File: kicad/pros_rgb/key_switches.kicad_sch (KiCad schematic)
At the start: 0 parts

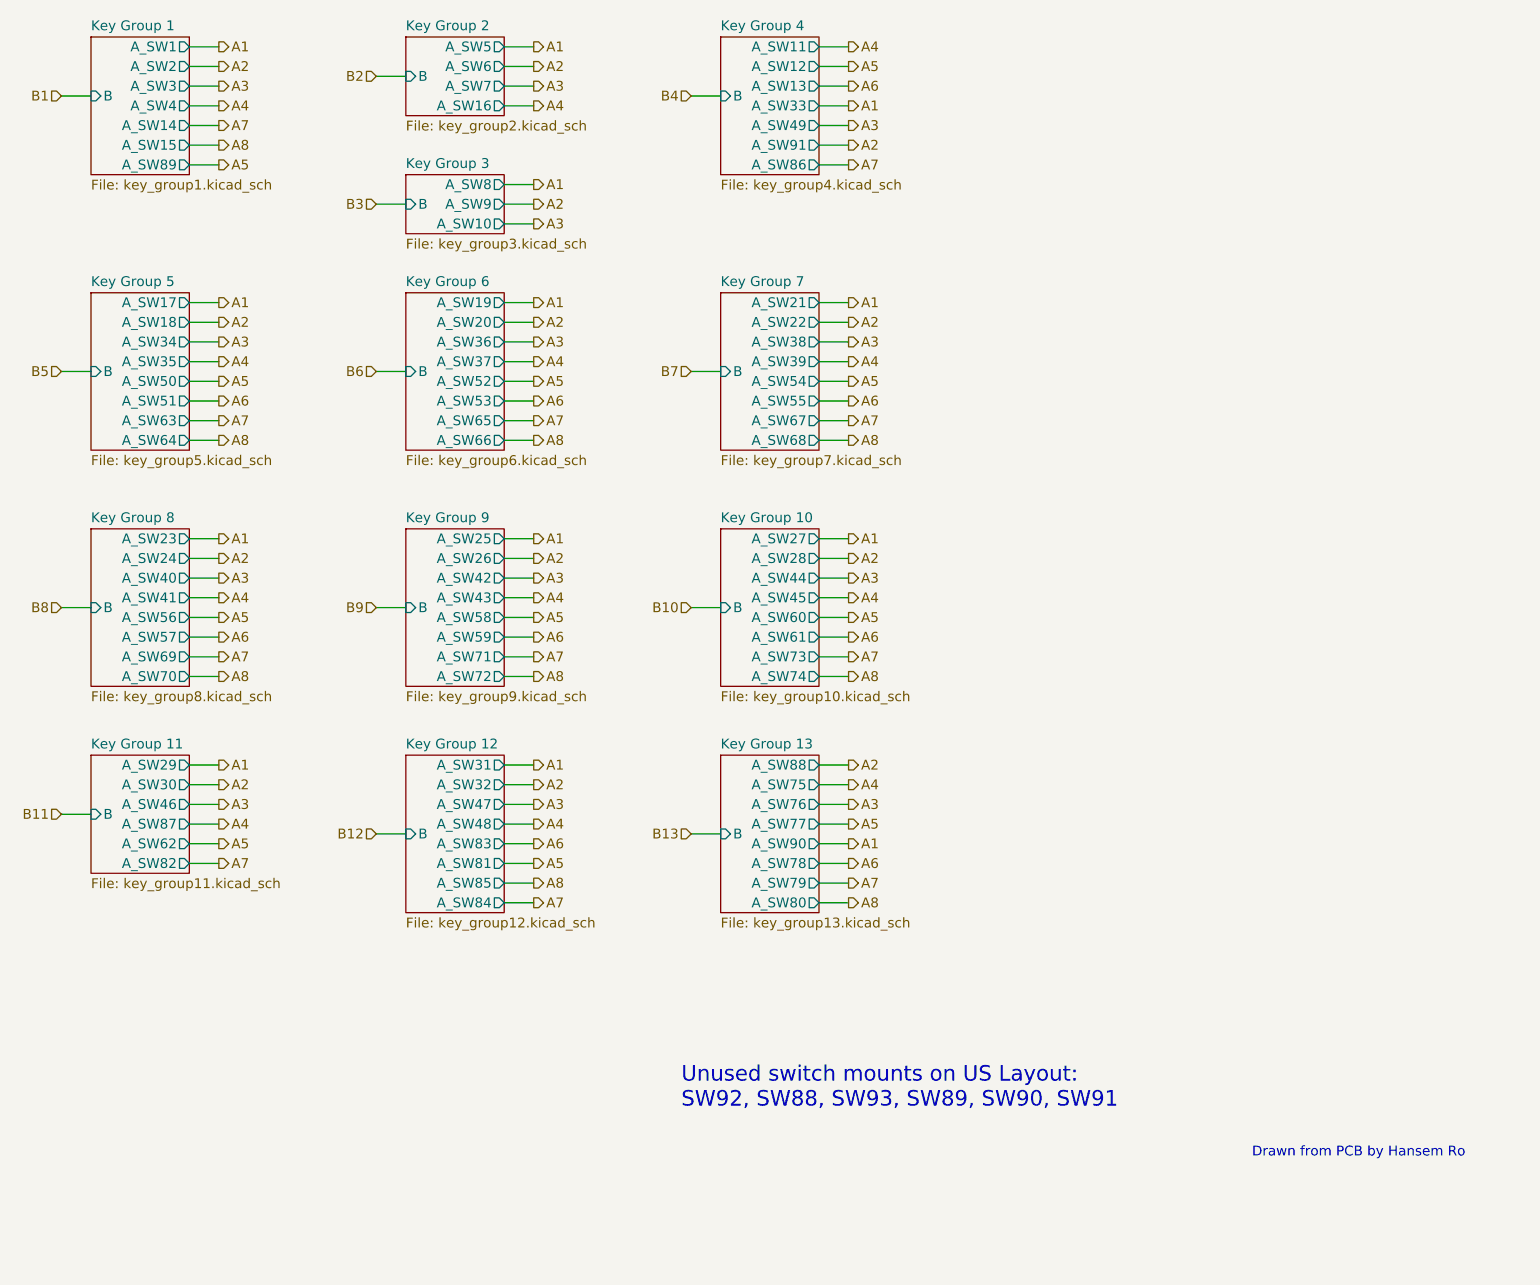
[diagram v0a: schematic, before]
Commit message: kicad/pros_rgb: update key groupings
These new groupings are based off ordering in firmware:
https://github.com/hansemro/pok3r_re_firmware/blob/4b68aa4baf7d28dc8dbf8eebcb1fdb59e7bcd629/disassemble/cmprosrgb/v122/cmprosrgb_v122.txt#L14599-L14629
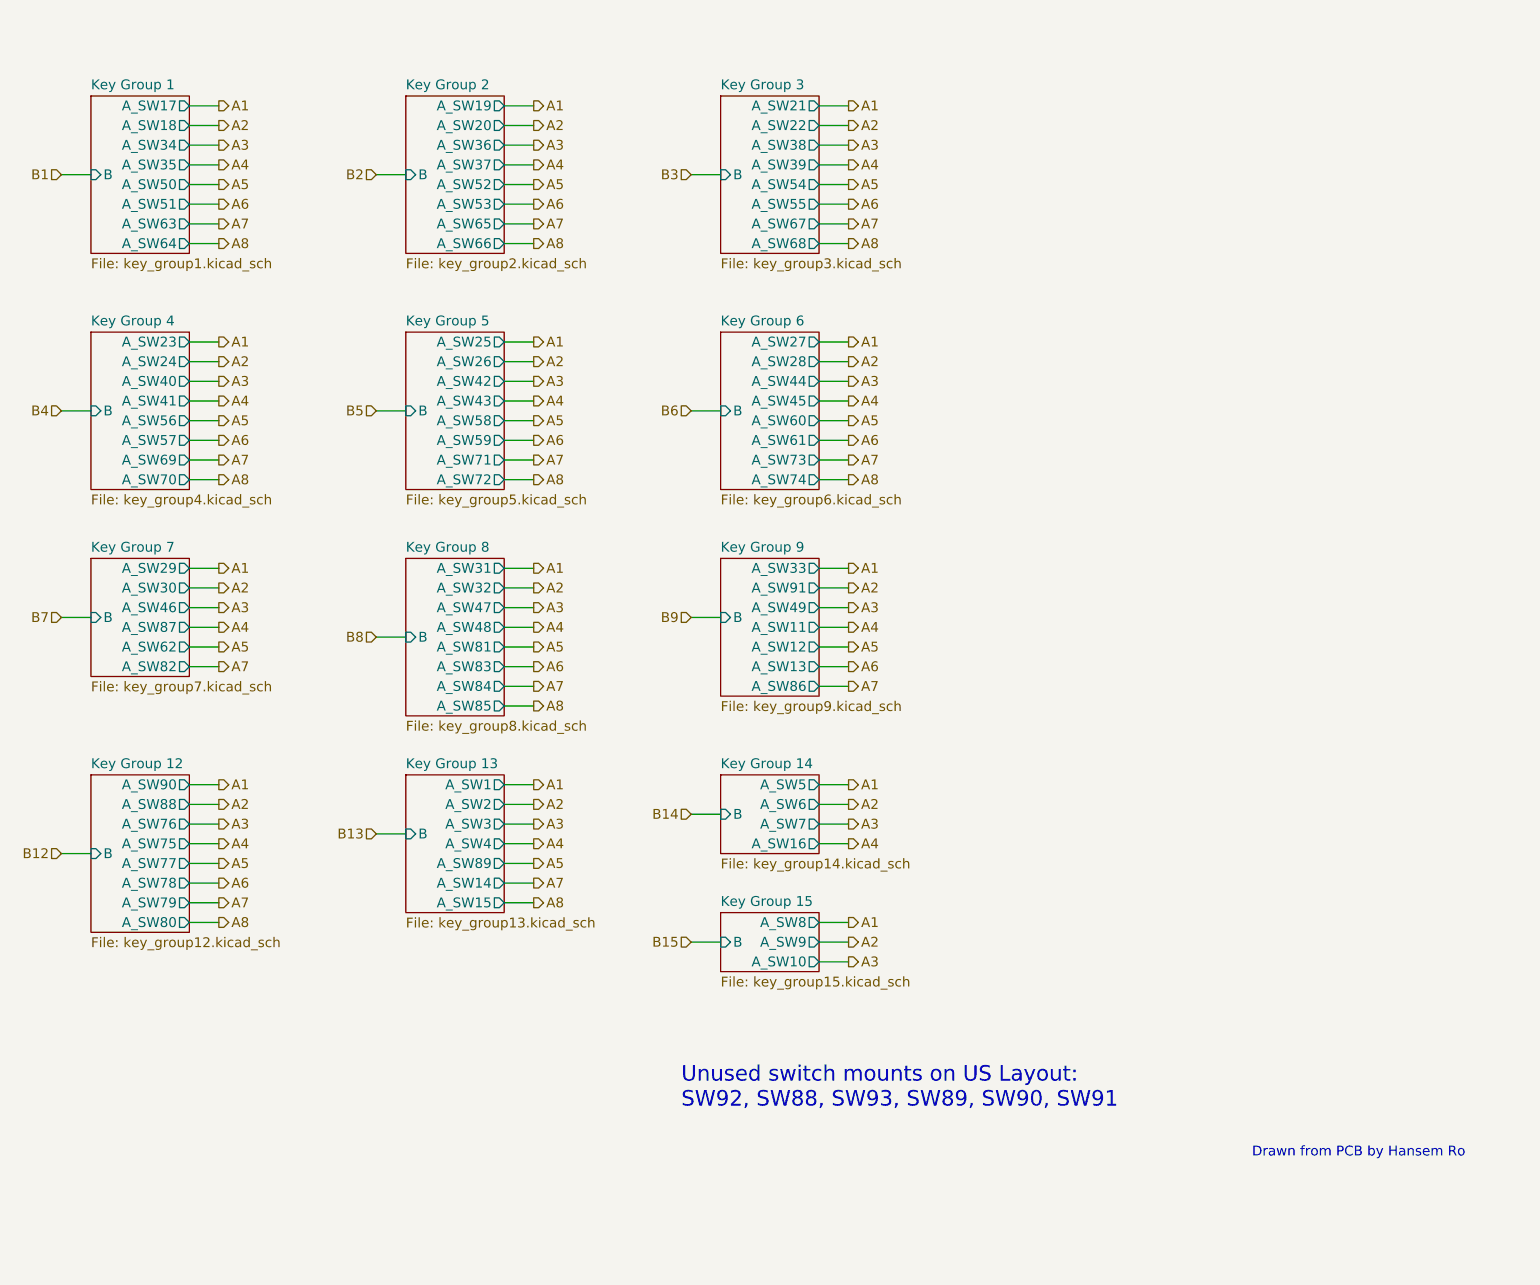
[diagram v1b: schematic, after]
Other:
- removed sheet Key Group 10
- removed sheet Key Group 11
- added sheet Key Group 14 (key_group14.kicad_sch)
- added sheet Key Group 15 (key_group15.kicad_sch)
- sheet Key Group 1 ports: added A_SW17, A_SW18, A_SW34, A_SW35, A_SW50, A_SW51, A_SW63, A_SW64; removed A_SW1, A_SW14, A_SW15, A_SW2, A_SW3, A_SW4, A_SW89
- sheet Key Group 12 ports: added A_SW75, A_SW76, A_SW77, A_SW78, A_SW79, A_SW80, A_SW88, A_SW90; removed A_SW31, A_SW32, A_SW47, A_SW48, A_SW81, A_SW83, A_SW84, A_SW85
- sheet Key Group 13 ports: added A_SW1, A_SW14, A_SW15, A_SW2, A_SW3, A_SW4, A_SW89; removed A_SW75, A_SW76, A_SW77, A_SW78, A_SW79, A_SW80, A_SW88, A_SW90
- sheet Key Group 2 ports: added A_SW19, A_SW20, A_SW36, A_SW37, A_SW52, A_SW53, A_SW65, A_SW66; removed A_SW16, A_SW5, A_SW6, A_SW7
- sheet Key Group 3 ports: added A_SW21, A_SW22, A_SW38, A_SW39, A_SW54, A_SW55, A_SW67, A_SW68; removed A_SW10, A_SW8, A_SW9
- sheet Key Group 4 ports: added A_SW23, A_SW24, A_SW40, A_SW41, A_SW56, A_SW57, A_SW69, A_SW70; removed A_SW11, A_SW12, A_SW13, A_SW33, A_SW49, A_SW86, A_SW91
- sheet Key Group 5 ports: added A_SW25, A_SW26, A_SW42, A_SW43, A_SW58, A_SW59, A_SW71, A_SW72; removed A_SW17, A_SW18, A_SW34, A_SW35, A_SW50, A_SW51, A_SW63, A_SW64
- sheet Key Group 6 ports: added A_SW27, A_SW28, A_SW44, A_SW45, A_SW60, A_SW61, A_SW73, A_SW74; removed A_SW19, A_SW20, A_SW36, A_SW37, A_SW52, A_SW53, A_SW65, A_SW66
- sheet Key Group 7 ports: added A_SW29, A_SW30, A_SW46, A_SW62, A_SW82, A_SW87; removed A_SW21, A_SW22, A_SW38, A_SW39, A_SW54, A_SW55, A_SW67, A_SW68
- sheet Key Group 8 ports: added A_SW31, A_SW32, A_SW47, A_SW48, A_SW81, A_SW83, A_SW84, A_SW85; removed A_SW23, A_SW24, A_SW40, A_SW41, A_SW56, A_SW57, A_SW69, A_SW70
- sheet Key Group 9 ports: added A_SW11, A_SW12, A_SW13, A_SW33, A_SW49, A_SW86, A_SW91; removed A_SW25, A_SW26, A_SW42, A_SW43, A_SW58, A_SW59, A_SW71, A_SW72

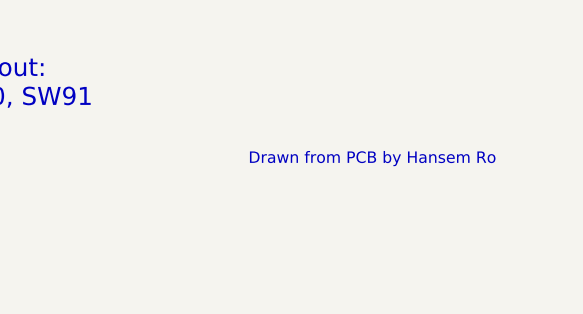
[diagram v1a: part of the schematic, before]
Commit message: kicad/pros_rgb: mark as Rev. B
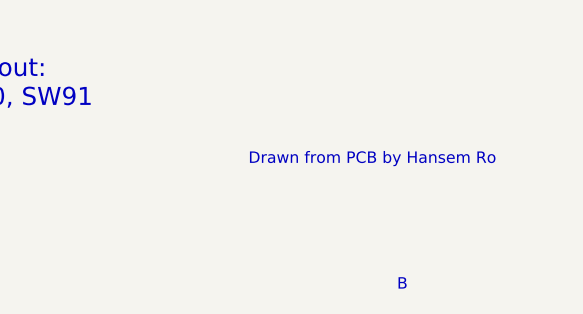
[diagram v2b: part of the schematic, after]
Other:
- note added: "B"
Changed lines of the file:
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@@
+    (effects (font (size 1.27 1.27)) (justify left bottom))
+  )
+  (text "B" (at 269.24 194.31 0)
     (effects (font (size 1.27 1.27)) (justify left bottom))
   )
